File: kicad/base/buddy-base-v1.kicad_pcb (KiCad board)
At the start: 4 copper layers, 238.8 x 128.5 mm, 76 parts, among them J1 USB_C_Receptacle, J10 Conn_01x06_Socket, J11 Conn_01x06_Socket, J12 Conn_01x06_Socket, J13 Conn_01x06_Socket, J14 Conn_01x06_Socket, J15 Conn_01x06, J16 Conn_01x06, J17 Conn_01x06, J18 Conn_01x06, J2 Conn_01x02_Socket, J3 Conn_01x06_Socket, J4 Conn_01x06_Socket, J5 Conn_01x06_Socket, J6 Conn_01x06_Socket, J7 Conn_01x06_Socket, J8 Conn_01x06_Socket, J9 Conn_01x06_Socket, Q2 AO3401A, SW1 SW_SPDT, U1 AP63203WU, U2 THVD1450DR, U3 ICE40UP5K-SG48ITR, U4 AP2127K-1.2, U5 W25Q32JVSS

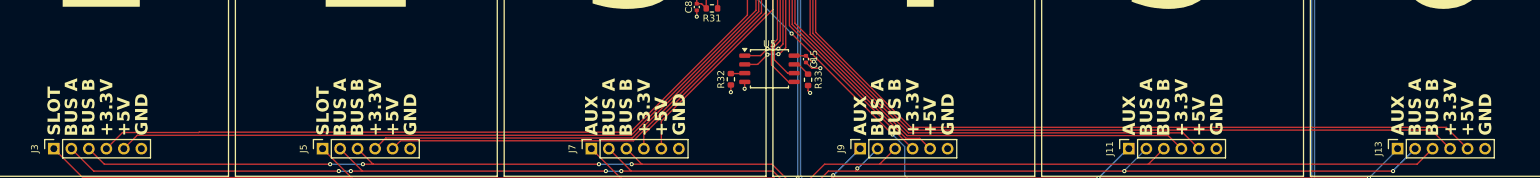
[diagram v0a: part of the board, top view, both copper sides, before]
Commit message: Update audio header labels
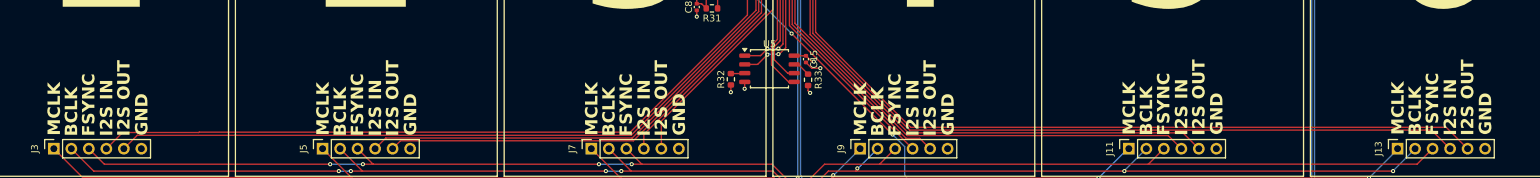
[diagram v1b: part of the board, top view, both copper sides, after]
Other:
- board text added: "I2S IN"
- board text added: "I2S OUT"

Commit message: Add new brains
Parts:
- added J19: TC2030, Connector:Tag-Connect_TC2030-IDC-NL_2x03_P1.27mm_Vertical, F.Cu at (150.0, 81.5)
- added R34: 10K, Resistor_SMD:R_0603_1608Metric, F.Cu at (219.3, 93.5)
- added TP1: TestPoint, TestPoint:TestPoint_THTPad_D1.0mm_Drill0.5mm, F.Cu at (144.6, 66.1)
- R32, R33: value R -> 10K
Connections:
- U3 pad 7: unconnected-(U3B-CDONE-Pad7) -> Net-(U3B-CDONE)
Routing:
- net FPGA_SPI_SS: track 14.9 -> 31.4 mm
- net FPGA_SPI_SCK: track 14.6 -> 23.0 mm
- net FPGA_SPI_SI: track 16.5 -> 23.6 mm
- net FPGA_SPI_SO: track 15.6 -> 20.7 mm
- net Net-(U3B-CDONE): track 0.00 -> 4.67 mm, vias 0 -> 1
- net RESET_1: track 86.3 -> 90.0 mm
- net 3V3_SYS: track 72.9 -> 75.8 mm, vias 19 -> 21
- net GND: track 77.8 -> 78.8 mm, vias 34 -> 35
